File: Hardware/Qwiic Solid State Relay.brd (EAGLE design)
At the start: 90.2 x 67.3 mm, 61 parts, among them J2 Qwiic Right Angle, J3 Qwiic Right Angle, J9 AVR_SPI_PROG_3X2TESTPOINTS, K1 25A Solid State Relay, K2 25A Solid State Relay, Q1 600mA/40V, Q2 600mA/40V, U4 ATTINY84-ARDUINO

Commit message: post review/checklist changes
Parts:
- removed U$1: (no value), buzzard_labels (16):DUAL_SOLID0
- removed U$4: (no value), buzzard_labels (16):STATE_RELAY1
- added D3, D4: (no value), SparkFun-LED:LED_5MM
- added J6: (no value), SparkFun-Connectors:1X01_NO_SILK
- added JP10, JP3, JP8: STAND-OFF, SparkFun-Hardware:STAND-OFF
- added LOGO4: QWIIC_LOGO_5MM, SparkFun-Aesthetics:QWIIC_5MM
- added R7, R8: 1k, SparkFun-Resistors:0603
- added U$11, U$12: (no value), SparkFun-Buzzard:RST_I
- added U$7, U$8: (no value), buzzard_labels (19):HIGH_VOLTAGE0
- ADR, PWR: value JUMPER-SMT_2_NO_SILK -> JUMPER-SMT_2_NC_TRACE_SILK; device SparkFun-Jumpers:SMT-JUMPER_2_NO_SILK -> SparkFun-Jumpers:SMT-JUMPER_2_NC_TRACE_SILK
- moved LOGO1 15.7 mm to (37.5, 17.8)
- moved ADR 8.00 mm to (48.0, 14.0)
- moved C5 8.00 mm to (53.1, 22.2)
- moved J9 8.00 mm to (53.1, 16.5)
- moved R17 8.00 mm to (53.1, 24.1)
- moved U$23 8.00 mm to (42.5, 14.0)
- moved U4 8.00 mm to (53.1, 16.5)
- moved U$10 2.16 mm to (60.6, 61.0)
- moved J1 1.27 mm to (15.2, 1.27)
- moved U$18 1.27 mm to (15.2, 1.91)
- moved U$19 1.27 mm to (15.2, 1.91)
- moved U$20 1.27 mm to (12.7, 1.91)
- moved U$21 1.27 mm to (12.7, 1.91)
- moved U$13 1.27 mm to (7.62, 1.52)
- moved U$14 1.27 mm to (7.62, 1.52)
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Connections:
- removed net N$1: D2.C, Q2.3, R5.1
- removed net N$2: D1.C, Q1.3, R2.1
- removed net RELAY_CTRL3: U4.12
- removed net RELAY_CTRL4: U4.13
- new net N$11: D1.C, D3.K, Q1.3, R2.1
- new net N$12: D3.A, R7.1
- new net N$17: D2.C, D4.K, Q2.3, R5.1
- new net N$18: D4.A, R8.1
- net !RESET: now also J6.1
- net 3.3V: now also R7.2, R8.2
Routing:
- net 3.3V: track 189.4 -> 241.7 mm, vias 7 -> 9
- net N$11: track 0.00 -> 48.9 mm
- net N$17: track 0.00 -> 48.6 mm
- net !RESET: track 9.28 -> 52.4 mm, vias 0 -> 1
- net RELAY_CTRL2: track 18.3 -> 10.3 mm
- net RELAY_CTRL1: track 36.1 -> 43.4 mm
- net N$18: track 0.00 -> 5.25 mm
- net N$12: track 0.00 -> 5.25 mm
- net N$2: track 4.38 -> 0.00 mm
- net N$1: track 4.38 -> 0.00 mm
- net N$3: track 22.9 -> 25.7 mm
- net SCL/SCK: track 96.4 -> 98.2 mm
- net SDA/MOSI: track 105.3 -> 107.0 mm
- net N$10: track 22.9 -> 21.9 mm
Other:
- outline, holes or cut-outs redrawn

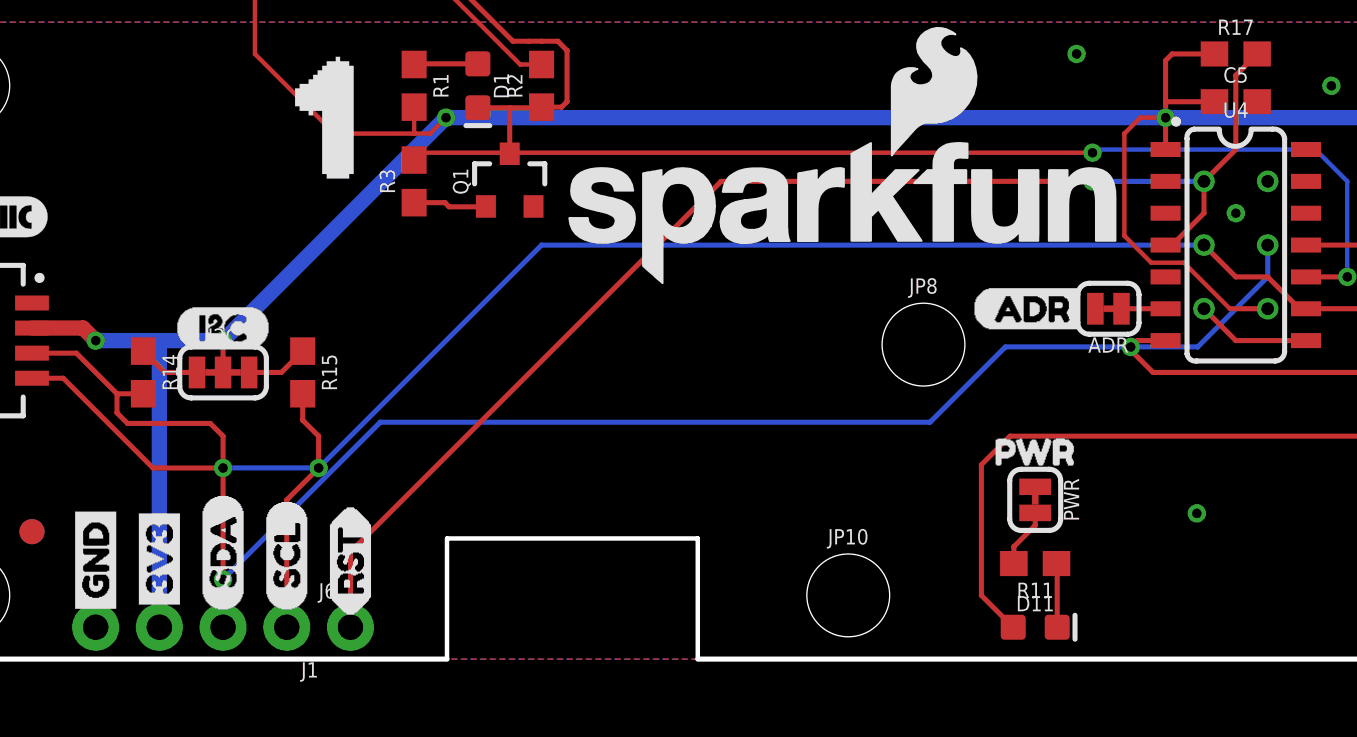
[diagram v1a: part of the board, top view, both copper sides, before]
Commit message: removing overlap errors
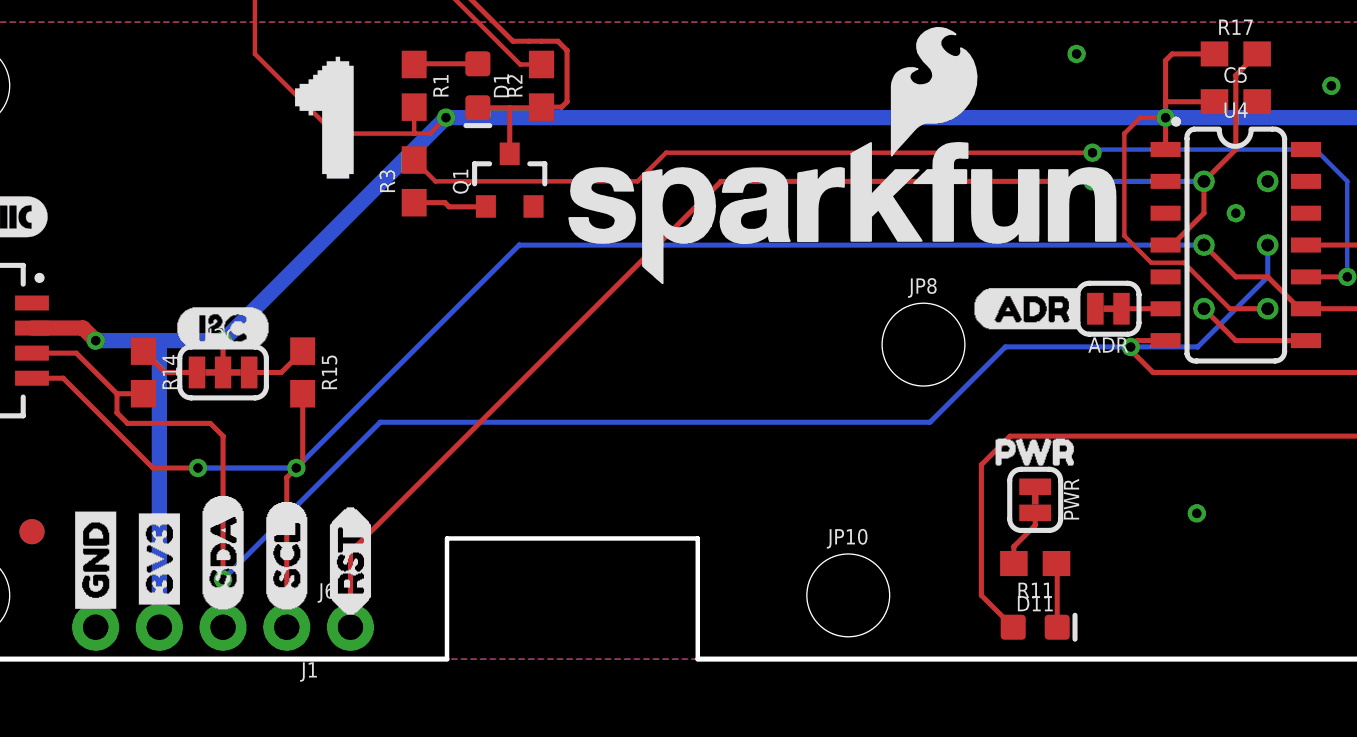
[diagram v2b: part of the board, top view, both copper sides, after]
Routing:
- net RELAY_CTRL1: track 43.4 -> 44.1 mm
- net SCL/SCK: track 98.2 -> 97.7 mm
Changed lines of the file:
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@@
 <wire x1="54.355" y1="15.24" x2="53.085" y2="15.24" width="0.2032" layer="1"/>
 <wire x1="53.085" y1="15.24" x2="51.815" y2="16.51" width="0.2032" layer="1"/>
-<wire x1="51.815" y1="16.51" x2="25.4" y2="16.51" width="0.2032" layer="16"/>
-<wire x1="25.4" y1="16.51" x2="16.51" y2="7.62" width="0.2032" layer="16"/>
-<via x="16.51" y="7.62" extent="1-16" drill="0.381"/>
-<wire x1="16.51" y1="7.62" x2="15.24" y2="6.35" width="0.2032" layer="1"/>
-<wire x1="15.24" y1="6.35" x2="15.24" y2="1.27" width="0.2032" layer="1"/>
+<wire x1="51.815" y1="16.51" x2="24.511" y2="16.51" width="0.2032" layer="16"/>
+<wire x1="24.511" y1="16.51" x2="15.621" y2="7.62" width="0.2032" layer="16"/>
+<via x="15.621" y="7.62" extent="1-16" drill="0.381"/>
+<wire x1="15.621" y1="7.62" x2="15.24" y2="7.239" width="0.2032" layer="1"/>
+<wire x1="15.24" y1="7.239" x2="15.24" y2="1.27" width="0.2032" layer="1"/>
 <contactref element="R15" pad="2"/>
-<wire x1="16.51" y1="7.62" x2="16.51" y2="8.89" width="0.2032" layer="1"/>
-<wire x1="15.875" y1="9.525" x2="15.875" y2="10.58" width="0.2032" layer="1"/>
-<wire x1="16.51" y1="8.89" x2="15.875" y2="9.525" width="0.2032" layer="1"/>
+<wire x1="15.875" y1="10.58" x2="15.875" y2="7.874" width="0.2032" layer="1"/>
+<wire x1="15.621" y1="7.62" x2="15.875" y2="7.874" width="0.2032" layer="1"/>
 <wire x1="5.08" y1="11.2" x2="6.326" y2="11.2" width="0.2032" layer="1"/>
-<via x="12.7" y="7.62" extent="1-16" drill="0.381"/>
+<via x="11.7" y="7.62" extent="1-16" drill="0.381"/>
 <wire x1="6.326" y1="11.2" x2="9.906" y2="7.62" width="0.2032" layer="1"/>
-<wire x1="9.906" y1="7.62" x2="12.7" y2="7.62" width="0.2032" layer="1"/>
-<wire x1="12.7" y1="7.62" x2="16.51" y2="7.62" width="0.2032" layer="16"/>
+<wire x1="9.906" y1="7.62" x2="11.7" y2="7.62" width="0.2032" layer="1"/>
+<wire x1="11.7" y1="7.62" x2="15.621" y2="7.62" width="0.2032" layer="16"/>
 <wire x1="55.885" y1="13.97" x2="65.8476375" y2="13.97" width="0.2032" layer="1"/>
 <wire x1="80.92981875" y1="16.383" x2="83.11281875" y2="14.2" width="0.2032" layer="1"/>
@@
 <contactref element="U4" pad="10"/>
 <contactref element="R3" pad="2"/>
-<wire x1="47.37" y1="20.193" x2="20.613" y2="20.193" width="0.1778" layer="1"/>
-<wire x1="20.32" y1="19.9" x2="20.613" y2="20.193" width="0.1778" layer="1"/>
+<wire x1="47.37" y1="20.193" x2="30.37" y2="20.193" width="0.1778" layer="1"/>
+<wire x1="30.37" y1="20.193" x2="29.227" y2="19.05" width="0.1778" layer="1"/>
+<wire x1="29.227" y1="19.05" x2="21.17" y2="19.05" width="0.1778" layer="1"/>
+<wire x1="20.32" y1="19.9" x2="21.17" y2="19.05" width="0.1778" layer="1"/>
 <via x="47.37" y="20.193" extent="1-16" drill="0.381"/>
 <wire x1="47.37" y1="20.193" x2="47.497" y2="20.32" width="0.1778" layer="16"/>
